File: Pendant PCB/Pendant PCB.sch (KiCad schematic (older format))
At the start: 30 parts, among them J1 Conn_01x20, J2 Conn_01x20, J3 Conn_02x04_Counter_Clockwise, J4 Conn_01x05

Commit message: PCB prepared. Drawings updated
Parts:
- removed J3: Conn_02x04_Counter_Clockwise, Connector_PinHeader_2.54mm:PinHeader_2x04_P2.54mm_Vertical, symbol Connector_Generic:Conn_02x04_Counter_Clockwise
- added H1, H2, H3, H4, H5, H6: MountingHole, MountingHole:MountingHole_2.5mm, symbol Mechanical:MountingHole
- added J5: Conn_02x02_Odd_Even, Connector_PinHeader_2.54mm:PinHeader_2x02_P2.54mm_Vertical, symbol Connector_Generic:Conn_02x02_Odd_Even
- EN_FEED1: renamed from SW_FEED1; footprint Rotary_Encoder:RotaryEncoder_Alps_EC12E-Switch_Vertical_H20mm -> Encoder:PEC11R-4x15K
- EN_JOG_X1: renamed from SW_X-JOG1; footprint Rotary_Encoder:RotaryEncoder_Alps_EC12E-Switch_Vertical_H20mm -> Encoder:PEC11R-4x15K
- EN_JOG_Y1: renamed from SW_Y-JOG1; footprint Rotary_Encoder:RotaryEncoder_Alps_EC12E-Switch_Vertical_H20mm -> Encoder:PEC11R-4x15K
- EN_JOG_Z1: renamed from SW_Z-JOG1; footprint Rotary_Encoder:RotaryEncoder_Alps_EC12E-Switch_Vertical_H20mm -> Encoder:PEC11R-4x15K
- EN_SPINDLE1: renamed from SW_SPINDLE1; footprint Rotary_Encoder:RotaryEncoder_Alps_EC12E-Switch_Vertical_H20mm -> Encoder:PEC11R-4x15K
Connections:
- net labels added: FA, FB, FR, HA, HLD, HX, HY, HZ, J_SW, J_X, J_Y, M1, M2, M3, M4, ML, MR, PX+, PX-, PY+, PY-, PZ-, RST, SA, SB, SR, STR, SW_F, SW_S, SW_X, SW_Y, SW_Z, UL, XA, XB, YA, YB, ZA, ZB
- wire segments 146 -> 166
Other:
- moved on the sheet: J4, SW_$H1, SW_$X1, SW_L-CLICK1, SW_MACRO-2, SW_MACRO-3, SW_MACRO-4, SW_R-CLICK1

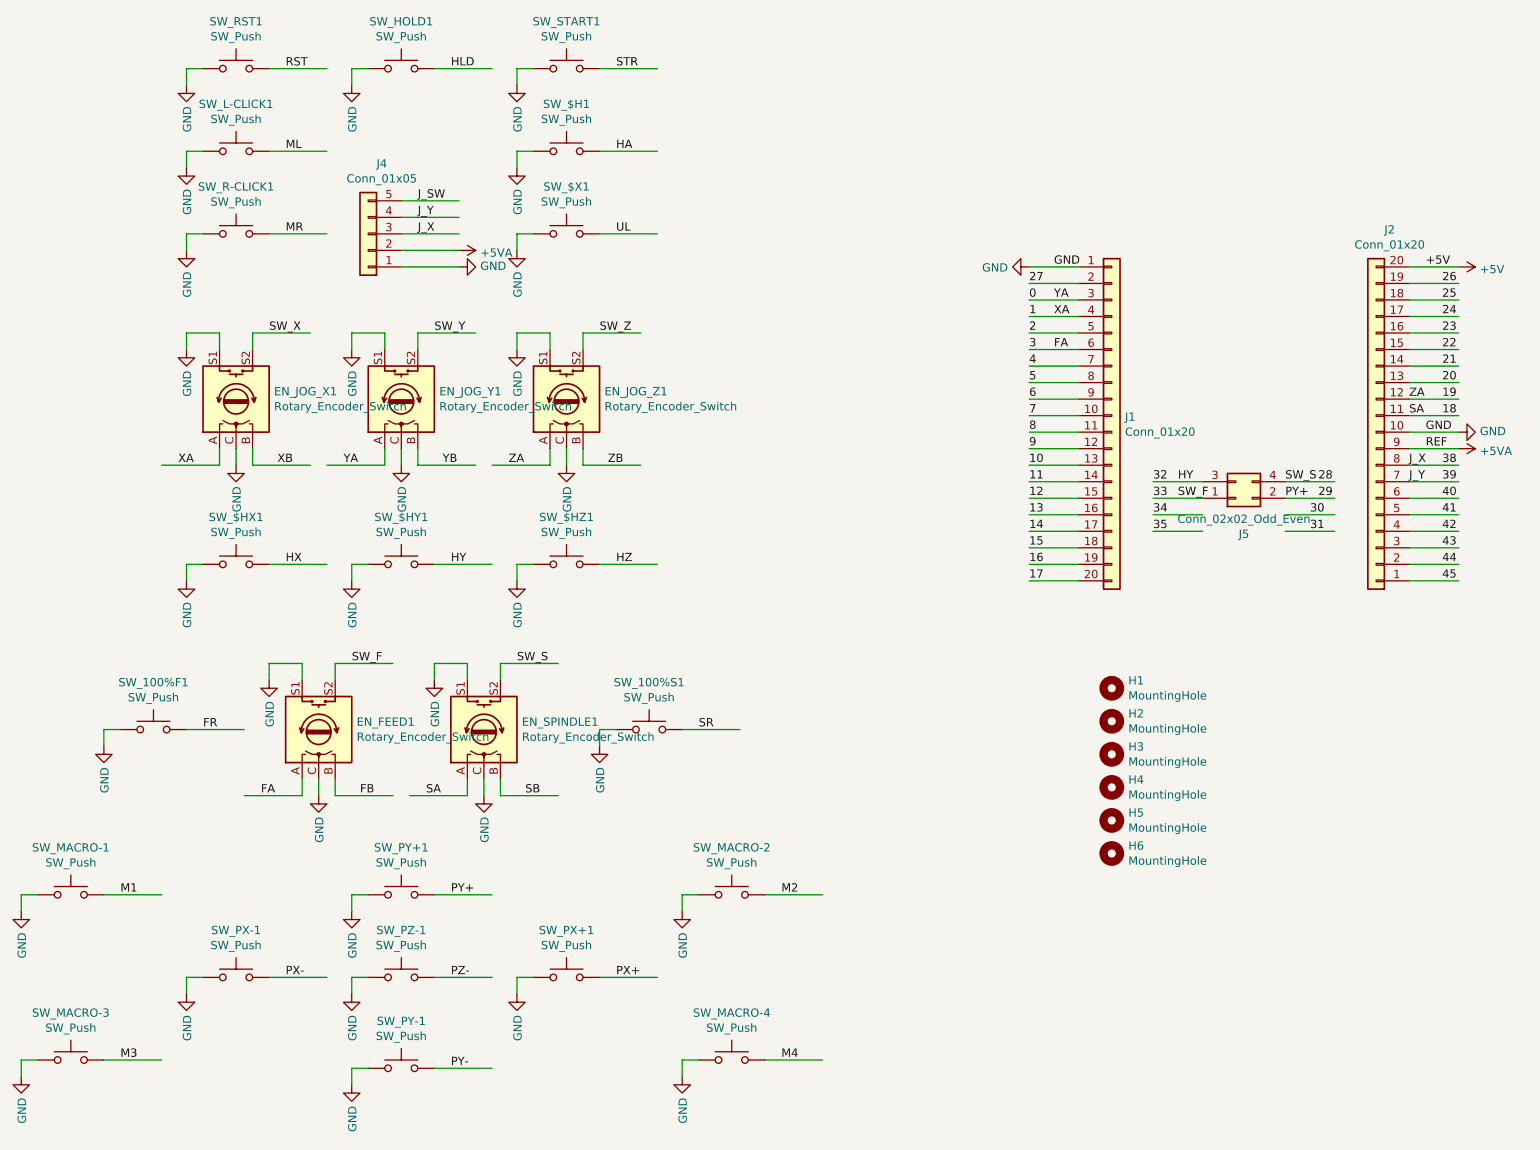
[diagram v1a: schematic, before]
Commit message: PCB routed. Feed and Spindle encoders moved .5mm closer to Y-axis
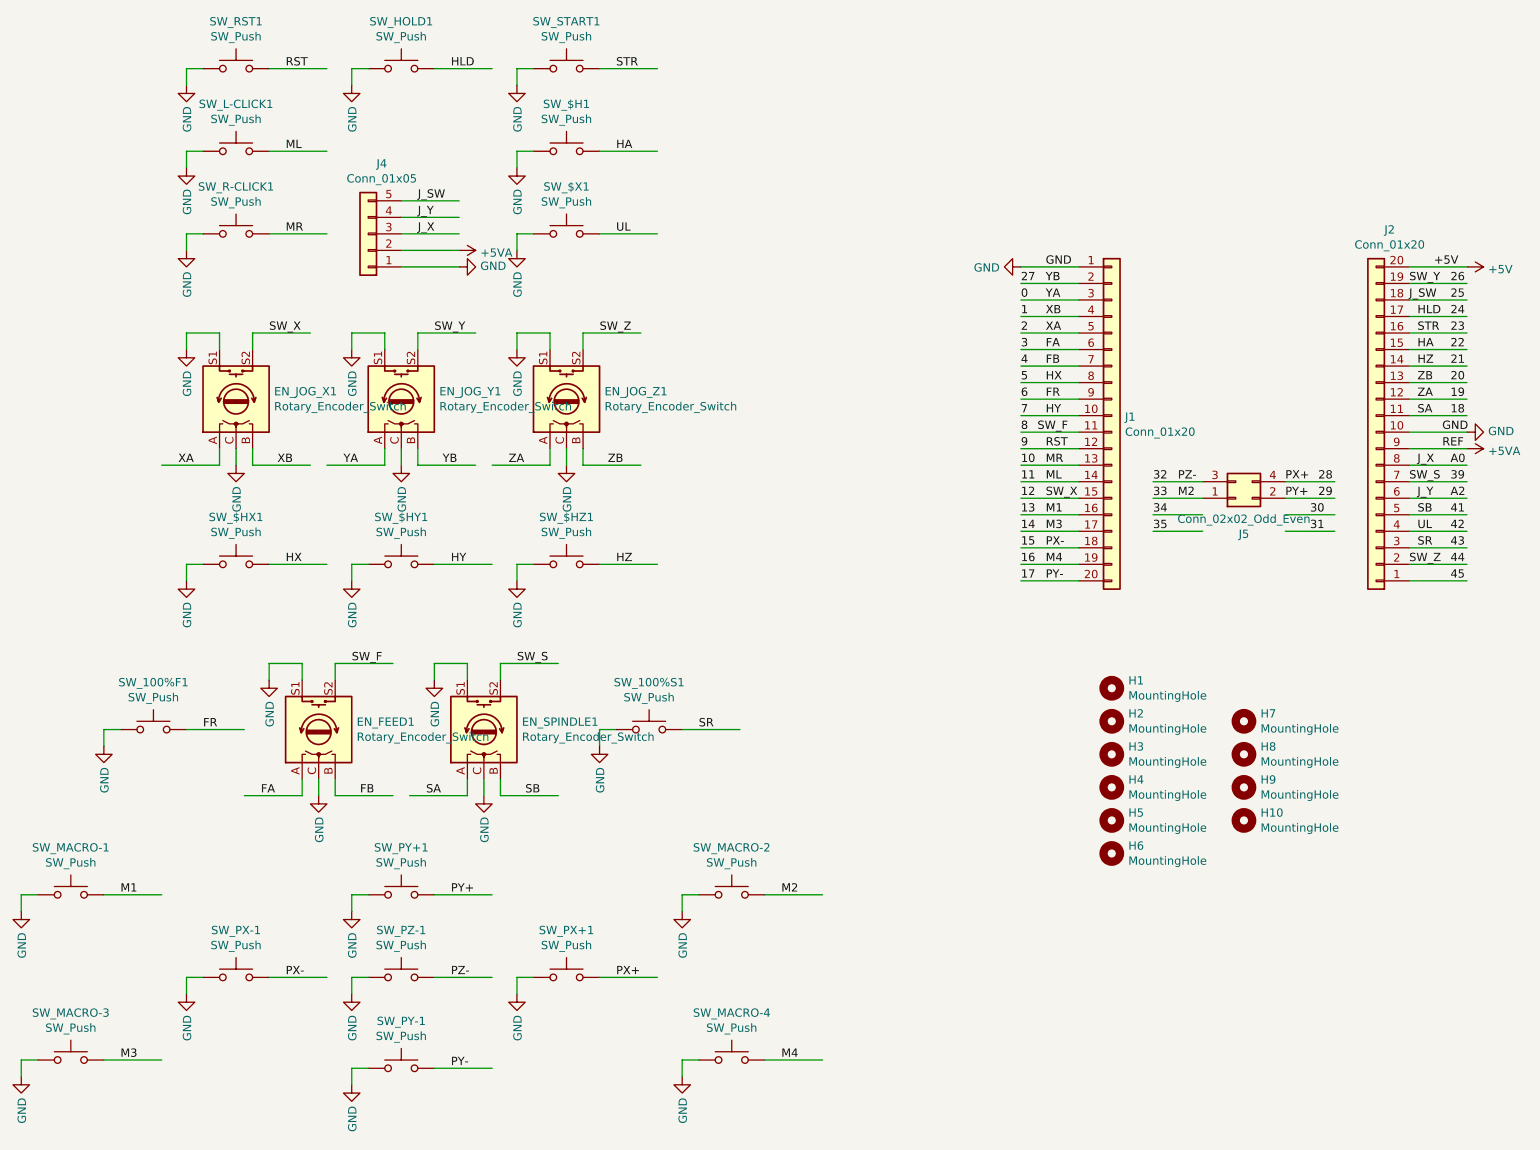
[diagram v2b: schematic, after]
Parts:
- added H10, H7, H8, H9: MountingHole, MountingHole:MountingHole_3.2mm_M3, symbol Mechanical:MountingHole
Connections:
- net labels added: A0, A2
- net labels removed: 38, 40
